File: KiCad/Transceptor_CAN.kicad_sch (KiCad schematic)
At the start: 5 parts

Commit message: Solucionando problemas del esquematic
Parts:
- removed C?: 4.7 nF, symbol Device:C
- removed J?: CAN BUS Connector, symbol Connector:Conn_01x02_Pin
- removed U?: SN65HVD230, Package_SO:SOIC-8_3.9x4.9mm_P1.27mm, symbol Interface_CAN_LIN:SN65HVD230
- added C3: 4.7 nF, symbol Device:C
- added J1: CAN BUS Connector, symbol Connector:Conn_01x02_Pin
- added U2: SN65HVD230, Package_SO:SOIC-8_3.9x4.9mm_P1.27mm, symbol Interface_CAN_LIN:SN65HVD230
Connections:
- net GND: now also C3.1, U2.2 (GND), U2.8 (Rs)
- net RXD: now also U2.4 (R)
- net TXD: now also U2.1 (D)
- net VCC: now also U2.3 (VCC)
- net at R?.1: now also J1.1 (Pin_1), U2.6 (CANL)
- net at R?.1, R?.2: now also C3.2
- net at R?.2: now also J1.2 (Pin_2), U2.7 (CANH)
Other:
- title: edd-project-grup-dimecres-dc_d_llums -> Transceptor_CAN

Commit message: Programador
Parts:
- removed U2: SN65HVD230, Package_SO:SOIC-8_3.9x4.9mm_P1.27mm, symbol Interface_CAN_LIN:SN65HVD230
- added U6: SN65HVD232, Package_SO:SOIC-8_3.9x4.9mm_P1.27mm, symbol Interface_CAN_LIN:SN65HVD232
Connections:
- net GND: now also U6.2 (GND)
- net RXD: now also U6.4 (R)
- net TXD: now also U6.1 (D)
- net VCC: now also U6.3 (VCC)
- net at J1.1 (Pin_1), R?.1: now also U6.6 (CANL)
- net at J1.2 (Pin_2), R?.2: now also U6.7 (CANH)
- no-connect marks 1 -> 0
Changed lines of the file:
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@@
 		(color 0 0 0 0)
-	)
-	(no_connect
-		(at 105.41 54.61)
 	)
 	(wire
@@
 	(wire
 		(pts
-			(xy 105.41 50.8) (xy 105.41 52.07)
-		)
-		(stroke
-			(width 0)
-			(type default)
-		)
-	)
-	(wire
-		(pts
 			(xy 85.09 66.04) (xy 85.09 57.15)
 		)
@@
 			(type dash)
 			(color 0 0 0 1)
-		)
-	)
-	(wire
-		(pts
-			(xy 107.95 50.8) (xy 105.41 50.8)
-		)
-		(stroke
-			(width 0)
-			(type default)
 		)
 	)
@@
 	(symbol
 		(lib_id "power:GND")
-		(at 107.95 50.8 0)
-		(unit 1)
-		(exclude_from_sim no)
-		(in_bom yes)
-		(on_board yes)
-		(dnp no)
-		(property "Reference" "#PWR09"
-			(at 107.95 57.15 0)
-			(effects
-				(font
-					(size 1.27 1.27)
-				)
-				(hide yes)
-			)
-		)
-		(property "Value" "GND"
-			(at 110.49 50.8 0)
-			(effects
-				(font
-					(size 1.27 1.27)
-				)
-			)
-		)
-		(property "Footprint" ""
-			(at 107.95 50.8 0)
-			(effects
-				(font
-					(size 1.27 1.27)
-				)
-				(hide yes)
-			)
-		)
-		(property "Datasheet" ""
-			(at 107.95 50.8 0)
-			(effects
-				(font
-					(size 1.27 1.27)
-				)
-				(hide yes)
-			)
-		)
-		(property "Description" "Power symbol creates a global label with name \"GND\" , ground"
-			(at 107.95 50.8 0)
-			(effects
-				(font
-					(size 1.27 1.27)
-				)
-				(hide yes)
-			)
-		)
-		(pin "1"
-		)
-		(instances
-			(project "Grup_D_Llums"
-				(path "/88ef36bc-9439-47f2-adb5-e1da6bb8c9dd/e1e92aea-0d85-4c86-995f-7fd094f12fbd"
-					(reference "#PWR09")
-					(unit 1)
-				)
-			)
-		)
-	)
-	(symbol
-		(lib_id "power:GND")
 		(at 58.42 46.99 0)
 		(unit 1)
@@
 	)
 	(symbol
-		(lib_id "Interface_CAN_LIN:SN65HVD230")
+		(lib_id "Interface_CAN_LIN:SN65HVD232")
 		(at 95.25 57.15 180)
 		(unit 1)
@@
 		(dnp no)
 		(fields_autoplaced yes)
-		(property "Reference" "U2"
+		(property "Reference" "U6"
 			(at 98.3681 44.45 0)
 			(effects
@@
 			)
 		)
-		(property "Value" "SN65HVD230"
+		(property "Value" "SN65HVD232"
 			(at 98.3681 46.99 0)
 			(effects
@@
 			)
 		)
-		(property "Description" "CAN Bus Transceivers, 3.3V, 1Mbps, Low-Power capabilities, SOIC-8"
+		(property "Description" "CAN Bus Transceivers, 3.3V, 1Mbps, SOIC-8"
 			(at 95.25 57.15 0)
 			(effects
@@
 			)
 		)
+		(pin "3"
+		)
+		(pin "2"
+		)
+		(pin "8"
+		)
+		(pin "1"
+		)
+		(pin "5"
+		)
+		(pin "6"
+		)
 		(pin "7"
 		)
-		(pin "2"
-		)
-		(pin "6"
-		)
-		(pin "5"
-		)
 		(pin "4"
 		)
-		(pin "8"
-		)
-		(pin "3"
-		)
-		(pin "1"
-		)
 		(instances
-			(project "Grup_D_Llums"
+			(project ""
 				(path "/88ef36bc-9439-47f2-adb5-e1da6bb8c9dd/e1e92aea-0d85-4c86-995f-7fd094f12fbd"
-					(reference "U2")
+					(reference "U6")
 					(unit 1)
 				)

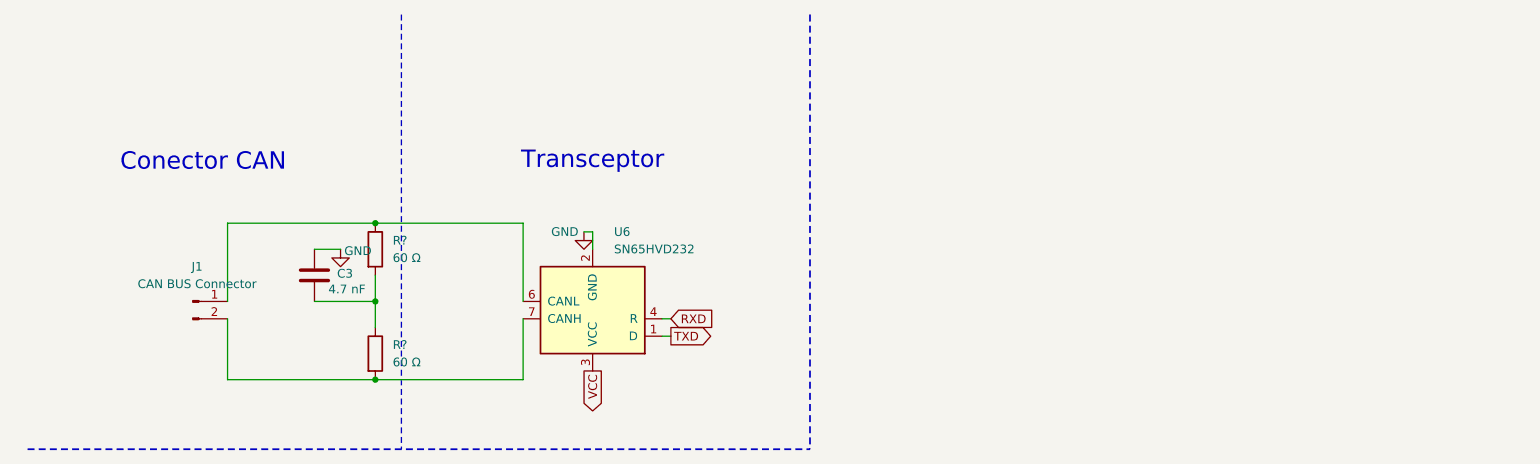
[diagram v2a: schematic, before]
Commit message: acabar can, estil y micro biel
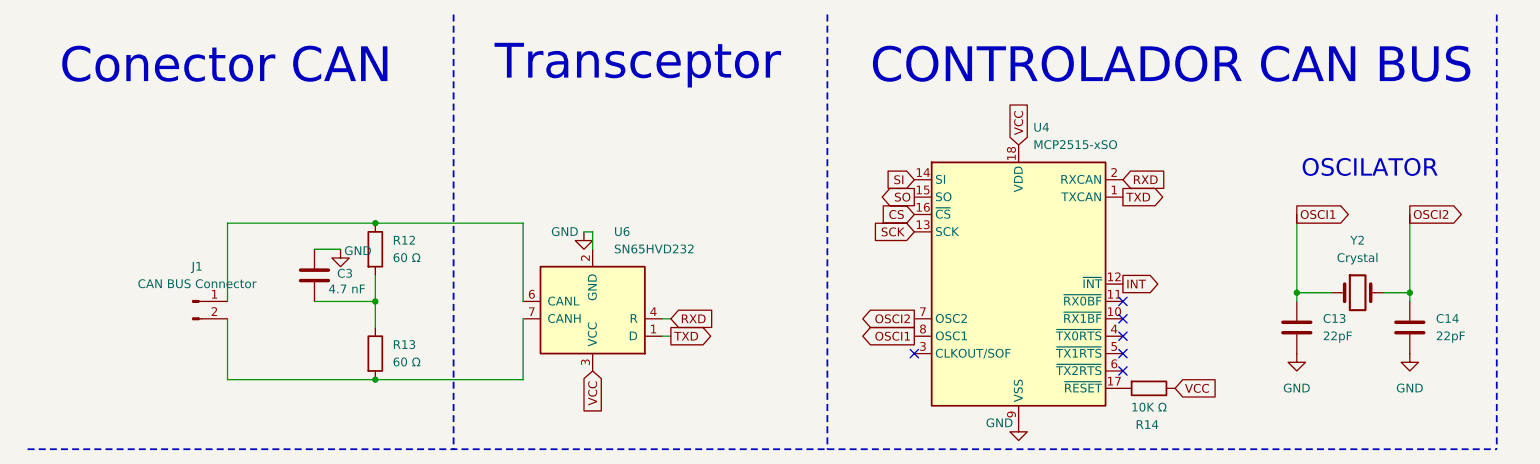
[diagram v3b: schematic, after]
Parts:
- added C13, C14: 22pF, Capacitor_SMD:C_0805_2012Metric, symbol Device:C
- added R14: 10K Ω, symbol Device:R
- added U4: MCP2515-xSO, Package_SO:SOIC-18W_7.5x11.6mm_P1.27mm, symbol Interface_CAN_LIN:MCP2515-xSO
- added Y2: Crystal, Crystal:Crystal_HC49-U_Vertical, symbol Device:Crystal
- gave numbers to parts that had none: 2
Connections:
- net GND: now also C13.2, C14.2, U4.9 (VSS)
- net RXD: now also U4.2 (RXCAN)
- net TXD: now also U4.1 (TXCAN)
- net VCC: now also R14.1, U4.18 (VDD)
- new net: R14.2, U4.17 (~{RESET})
- new net CS: U4.16 (~{CS})
- new net INT: U4.12 (~{INT})
- new net OSCI1: C13.1, U4.8 (OSC1), Y2.1
- new net OSCI2: C14.1, U4.7 (OSC2), Y2.2
- new net SCK: U4.13 (SCK)
- new net SI: U4.14 (SI)
- new net SO: U4.15 (SO)
- no-connect marks 0 -> 6
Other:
- note added: "CONTROLADOR CAN BUS"
- note added: "OSCILATOR"

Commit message: Debugging
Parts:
- removed J1: CAN BUS Connector, symbol Connector:Conn_01x02_Pin
- added J1: DE9_Pins, symbol Connector:DE9_Pins
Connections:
- net GND: now also J1.3
- net at R12.1: now also U6.7 (CANH), J1.7; no longer U6.6 (CANL)
- net at R13.2: now also U6.6 (CANL), J1.2; no longer U6.7 (CANH)
- no-connect marks 6 -> 12
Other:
- moved on the sheet: U6
